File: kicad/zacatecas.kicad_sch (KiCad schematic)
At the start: 53 parts, among them J1 LCD, J2 microSD, J3 CA1, J4 nanoLink, J5 STEP, J6 POWER, J7 SS22, Q1 BC548, Q2 BC548, Q3 BC548, SW1 RESET, SW10 7, SW2 NMI, SW3 3, SW4 1, SW5 0, SW6 2, SW7 4, SW8 6, SW9 5, U1 65C02, U2 65C22, U3 62256, U4 74HC132, U5 74HC32, U6 27C128, X1 1 MHz

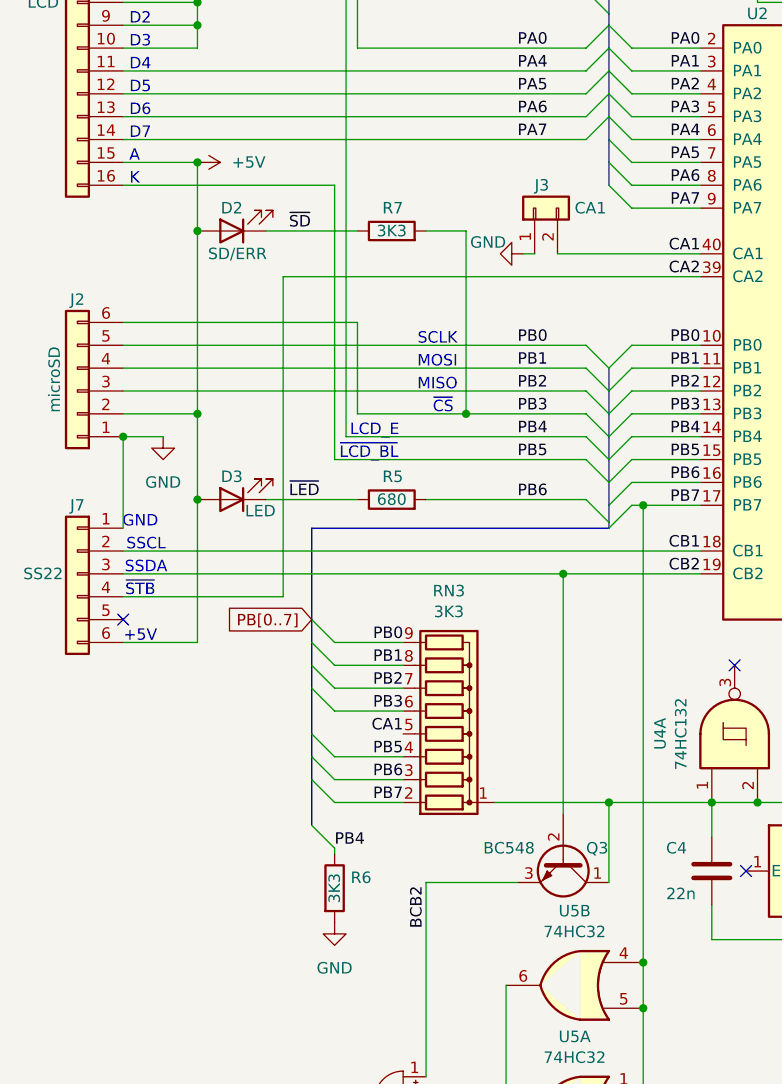
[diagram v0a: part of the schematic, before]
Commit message: fix LCD and add pad test
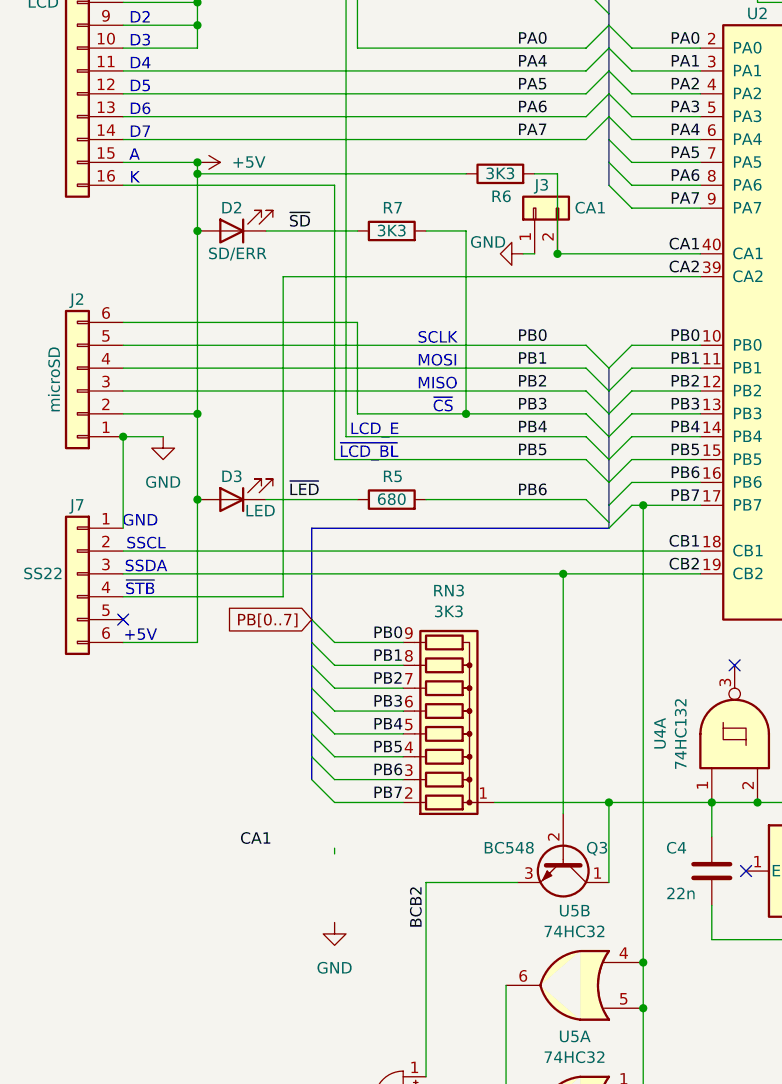
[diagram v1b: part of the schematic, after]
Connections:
- net +5V: now also R6.1
- net CA1: now also R6.2; no longer RN3.5 (R4)
- net GND: no longer R6.2
- net PB4: now also RN3.5 (R4); no longer R6.1
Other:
- moved on the sheet: R6
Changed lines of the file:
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@@
 	(title_block
 		(title "Zacatecas")
-		(date "2026-04-13")
-		(rev "v1")
+		(date "2026-08-08")
+		(rev "v1.1")
 		(company "@zuiko21")
 		(comment 1 "(c) 2026 Carlos J. Santisteban")
@@
 	)
 	(junction
+		(at 73.66 77.47)
+		(diameter 0)
+		(color 0 0 0 0)
+	)
+	(junction
 		(at 168.91 189.23)
 		(diameter 0)
@@
 	)
 	(junction
+		(at 33.655 68.58)
+		(diameter 0)
+		(color 0 0 0 0)
+	)
+	(junction
 		(at 161.925 137.16)
 		(diameter 0)
@@
 	)
 	(bus_entry
-		(at 46.355 140.97)
+		(at 46.355 128.27)
 		(size 2.54 2.54)
 		(stroke
@@
 	(bus
 		(pts
-			(xy 46.355 125.73) (xy 46.355 130.81)
+			(xy 46.355 125.73) (xy 46.355 128.27)
 		)
 		(stroke
@@
 	(wire
 		(pts
+			(xy 48.895 130.81) (xy 56.515 130.81)
+		)
+		(stroke
+			(width 0)
+			(type default)
+		)
+	)
+	(wire
+		(pts
 			(xy 33.655 104.775) (xy 33.655 120.65)
 		)
@@
 	(wire
 		(pts
+			(xy 73.66 68.58) (xy 73.66 77.47)
+		)
+		(stroke
+			(width 0)
+			(type default)
+		)
+	)
+	(wire
+		(pts
 			(xy 74.295 40.64) (xy 76.835 40.64)
 		)
@@
 		)
 	)
-	(bus
-		(pts
-			(xy 46.355 135.89) (xy 46.355 140.97)
-		)
-		(stroke
-			(width 0)
-			(type default)
-		)
-	)
 	(wire
 		(pts
@@
 	(wire
 		(pts
-			(xy 33.655 67.31) (xy 33.655 74.93)
+			(xy 33.655 67.31) (xy 33.655 68.58)
 		)
 		(stroke
@@
 	(wire
 		(pts
+			(xy 71.12 68.58) (xy 73.66 68.58)
+		)
+		(stroke
+			(width 0)
+			(type default)
+		)
+	)
+	(wire
+		(pts
 			(xy 127.635 113.03) (xy 114.935 113.03)
 		)
@@
 	(wire
 		(pts
+			(xy 33.655 68.58) (xy 63.5 68.58)
+		)
+		(stroke
+			(width 0)
+			(type default)
+		)
+	)
+	(wire
+		(pts
 			(xy 151.765 123.19) (xy 151.765 125.73)
 		)
@@
 		)
 	)
+	(bus
+		(pts
+			(xy 46.355 128.27) (xy 46.355 130.81)
+		)
+		(stroke
+			(width 0)
+			(type default)
+		)
+	)
 	(wire
 		(pts
@@
 	(wire
 		(pts
+			(xy 33.655 68.58) (xy 33.655 74.93)
+		)
+		(stroke
+			(width 0)
+			(type default)
+		)
+	)
+	(wire
+		(pts
 			(xy 136.525 80.01) (xy 128.905 80.01)
 		)
@@
 	)
 	(label "CA1"
-		(at 56.515 130.81 180)
+		(at 41.91 143.51 180)
 		(effects
 			(font
@@
 	)
 	(label "PB4"
-		(at 48.895 143.51 0)
+		(at 56.515 130.81 180)
 		(effects
 			(font
 				(size 1.27 1.27)
 			)
-			(justify left bottom)
+			(justify right bottom)
 		)
 	)
@@
 	(symbol
 		(lib_id "Device:R")
-		(at 48.895 147.955 0)
+		(at 67.31 68.58 90)
 		(unit 1)
 		(exclude_from_sim no)
@@
 		(dnp no)
 		(property "Reference" "R6"
-			(at 50.673 146.7866 0)
+			(at 68.58 71.12 90)
 			(effects
 				(font
@@
 		)
 		(property "Value" "3K3"
-			(at 48.895 147.955 90)
+			(at 67.31 68.58 90)
 			(effects
 				(font
@@
 		)
 		(property "Footprint" "Resistor_THT:R_Axial_DIN0207_L6.3mm_D2.5mm_P2.54mm_Vertical"
-			(at 47.117 147.955 90)
+			(at 67.31 70.358 90)
 			(effects
 				(font
@@
 		)
 		(property "Datasheet" "~"
-			(at 48.895 147.955 0)
+			(at 67.31 68.58 0)
 			(effects
 				(font
@@
 		)
 		(property "Description" ""
-			(at 48.895 147.955 0)
+			(at 67.31 68.58 0)
 			(effects
 				(font
